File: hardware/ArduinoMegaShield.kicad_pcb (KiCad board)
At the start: 2 copper layers, 42 parts, among them P1 CONN_01X02, P10 CONN_01X02, P11 CONN_01X02, P12 CONN_01X02, P13 CONN_01X02, P14 CONN_01X02, P15 CONN_01X02, P16 CONN_01X02, P17 CONN_01X02, P18 CONN_01X02, P19 CONN_01X02, P2 CONN_01X02, P20 CONN_01X02, P21 CONN_01X02, P22 CONN_01X02, P3 CONN_01X02, P4 CONN_01X02, P5 CONN_01X02, P6 CONN_01X02, P7 CONN_01X02, P8 CONN_01X02, P9 CONN_01X02, U1 A4988, U2 A4988, U3 A4988

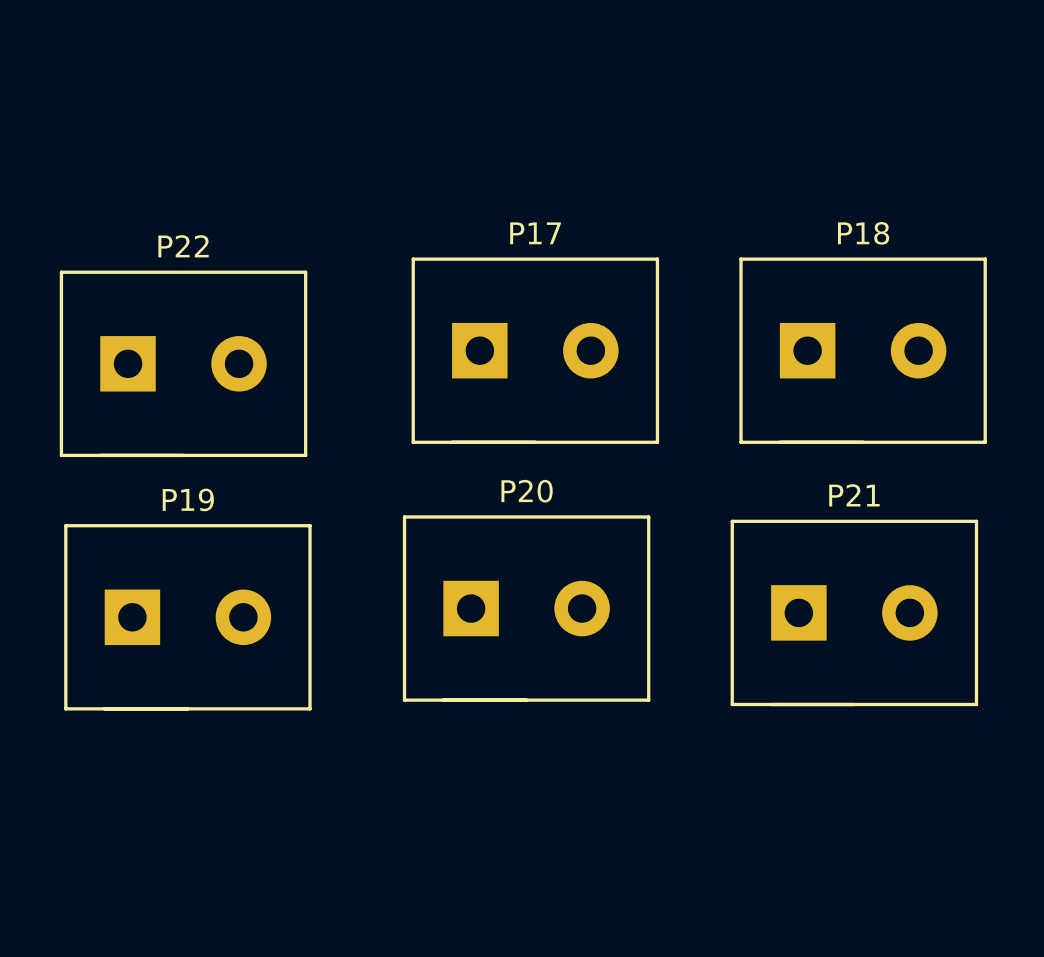
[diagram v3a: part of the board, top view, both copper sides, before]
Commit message: added NOPOPs for optional pullups on limit switches
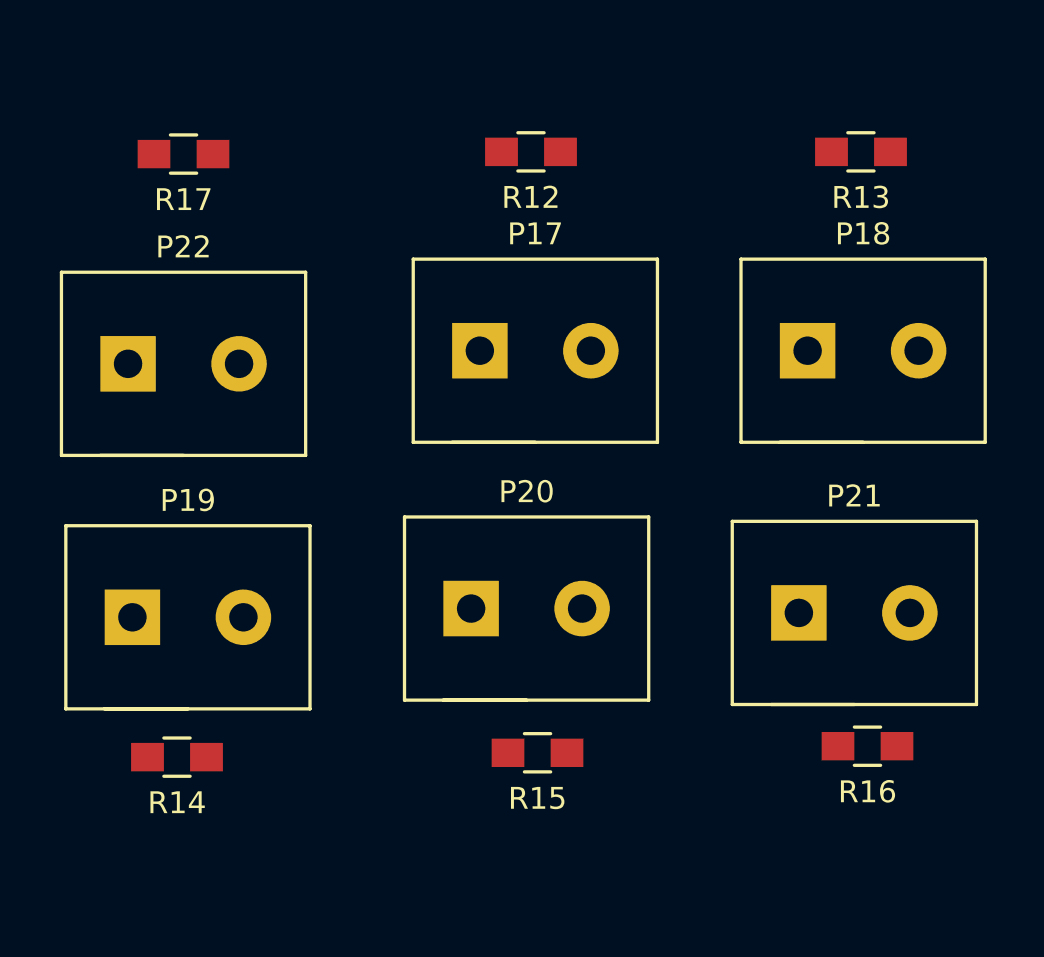
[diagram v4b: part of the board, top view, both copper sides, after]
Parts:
- added R12: NOPOP, Resistors_SMD:R_0805_HandSoldering, F.Cu at (170.0, 137.3)
- added R13: NOPOP, Resistors_SMD:R_0805_HandSoldering, F.Cu at (185.1, 137.3)
- added R14: NOPOP, Resistors_SMD:R_0805_HandSoldering, F.Cu at (153.8, 165.0)
- added R15: NOPOP, Resistors_SMD:R_0805_HandSoldering, F.Cu at (170.3, 164.8)
- added R16: NOPOP, Resistors_SMD:R_0805_HandSoldering, F.Cu at (185.4, 164.5)
- added R17: NOPOP, Resistors_SMD:R_0805_HandSoldering, F.Cu at (154.1, 137.4)
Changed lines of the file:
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@@
 (kicad_pcb (version 4) (host pcbnew 4.0.5)
   (general
-    (links 98)
-    (no_connects 93)
+    (links 110)
+    (no_connects 105)
     (area 0 0 0 0)
     (thickness 1.6)
@@
     (tracks 0)
     (zones 0)
-    (modules 42)
+    (modules 48)
     (nets 46)
   )
@@
       (at (xyz 0 0 0))
       (scale (xyz 1 1 1))
+      (rotate (xyz 0 0 0))
+    )
+  )
+  (module Resistors_SMD:R_0805_HandSoldering (layer F.Cu)
+    (at 170 137.3 180)
+    (descr "Resistor SMD 0805, hand soldering")
+    (tags "resistor 0805")
+    (attr smd)
+    (fp_text reference R12 (at 0 -2.1 180) (layer F.SilkS)
+      (effects (font (size 1 1) (thickness 0.15)))
+    )
+    (fp_text value NOPOP (at 0 2.1 180) (layer F.Fab)
+      (effects (font (size 1 1) (thickness 0.15)))
+    )
+    (fp_line (start -1 0.625) (end -1 -0.625) (layer F.Fab) (width 0.1))
+    (fp_line (start 1 0.625) (end -1 0.625) (layer F.Fab) (width 0.1))
+    (fp_line (start 1 -0.625) (end 1 0.625) (layer F.Fab) (width 0.1))
+    (fp_line (start -1 -0.625) (end 1 -0.625) (layer F.Fab) (width 0.1))
+    (fp_line (start -2.4 -1) (end 2.4 -1) (layer F.CrtYd) (width 0.05))
+    (fp_line (start -2.4 1) (end 2.4 1) (layer F.CrtYd) (width 0.05))
+    (fp_line (start -2.4 -1) (end -2.4 1) (layer F.CrtYd) (width 0.05))
+    (fp_line (start 2.4 -1) (end 2.4 1) (layer F.CrtYd) (width 0.05))
+    (fp_line (start 0.6 0.875) (end -0.6 0.875) (layer F.SilkS) (width 0.15))
+    (fp_line (start -0.6 -0.875) (end 0.6 -0.875) (layer F.SilkS) (width 0.15))
+    (pad 1 smd rect (at -1.35 0 180) (size 1.5 1.3) (layers F.Cu F.Paste F.Mask)
+      (net 7 +5V))
+    (pad 2 smd rect (at 1.35 0 180) (size 1.5 1.3) (layers F.Cu F.Paste F.Mask)
+      (net 40 /A_LIMIT))
+    (model Resistors_SMD.3dshapes/R_0805_HandSoldering.wrl
+      (at (xyz 0 0 0))
+      (scale (xyz 1 1 1))
+      (rotate (xyz 0 0 0))
+    )
+  )
+  (module Resistors_SMD:R_0805_HandSoldering (layer F.Cu)
+    (at 185.1 137.3 180)
+    (descr "Resistor SMD 0805, hand soldering")
+    (tags "resistor 0805")
+    (attr smd)
+    (fp_text reference R13 (at 0 -2.1 180) (layer F.SilkS)
+      (effects (font (size 1 1) (thickness 0.15)))
+    )
+    (fp_text value NOPOP (at 0 2.1 180) (layer F.Fab)
+      (effects (font (size 1 1) (thickness 0.15)))
+    )
+    (fp_line (start -1 0.625) (end -1 -0.625) (layer F.Fab) (width 0.1))
+    (fp_line (start 1 0.625) (end -1 0.625) (layer F.Fab) (width 0.1))
+    (fp_line (start 1 -0.625) (end 1 0.625) (layer F.Fab) (width 0.1))
+    (fp_line (start -1 -0.625) (end 1 -0.625) (layer F.Fab) (width 0.1))
+    (fp_line (start -2.4 -1) (end 2.4 -1) (layer F.CrtYd) (width 0.05))
+    (fp_line (start -2.4 1) (end 2.4 1) (layer F.CrtYd) (width 0.05))
+    (fp_line (start -2.4 -1) (end -2.4 1) (layer F.CrtYd) (width 0.05))
+    (fp_line (start 2.4 -1) (end 2.4 1) (layer F.CrtYd) (width 0.05))
+    (fp_line (start 0.6 0.875) (end -0.6 0.875) (layer F.SilkS) (width 0.15))
+    (fp_line (start -0.6 -0.875) (end 0.6 -0.875) (layer F.SilkS) (width 0.15))
+    (pad 1 smd rect (at -1.35 0 180) (size 1.5 1.3) (layers F.Cu F.Paste F.Mask)
+      (net 7 +5V))
+    (pad 2 smd rect (at 1.35 0 180) (size 1.5 1.3) (layers F.Cu F.Paste F.Mask)
+      (net 41 /X_LIMIT))
+    (model Resistors_SMD.3dshapes/R_0805_HandSoldering.wrl
+      (at (xyz 0 0 0))
+      (scale (xyz 1 1 1))
+      (rotate (xyz 0 0 0))
+    )
+  )
+  (module Resistors_SMD:R_0805_HandSoldering (layer F.Cu)
+    (at 153.8 165 180)
+    (descr "Resistor SMD 0805, hand soldering")
+    (tags "resistor 0805")
+    (attr smd)
+    (fp_text reference R14 (at 0 -2.1 180) (layer F.SilkS)
+      (effects (font (size 1 1) (thickness 0.15)))
+    )
+    (fp_text value NOPOP (at 0 2.1 180) (layer F.Fab)
+      (effects (font (size 1 1) (thickness 0.15)))
+    )
+    (fp_line (start -1 0.625) (end -1 -0.625) (layer F.Fab) (width 0.1))
+    (fp_line (start 1 0.625) (end -1 0.625) (layer F.Fab) (width 0.1))
+    (fp_line (start 1 -0.625) (end 1 0.625) (layer F.Fab) (width 0.1))
+    (fp_line (start -1 -0.625) (end 1 -0.625) (layer F.Fab) (width 0.1))
+    (fp_line (start -2.4 -1) (end 2.4 -1) (layer F.CrtYd) (width 0.05))
+    (fp_line (start -2.4 1) (end 2.4 1) (layer F.CrtYd) (width 0.05))
+    (fp_line (start -2.4 -1) (end -2.4 1) (layer F.CrtYd) (width 0.05))
+    (fp_line (start 2.4 -1) (end 2.4 1) (layer F.CrtYd) (width 0.05))
+    (fp_line (start 0.6 0.875) (end -0.6 0.875) (layer F.SilkS) (width 0.15))
+    (fp_line (start -0.6 -0.875) (end 0.6 -0.875) (layer F.SilkS) (width 0.15))
+    (pad 1 smd rect (at -1.35 0 180) (size 1.5 1.3) (layers F.Cu F.Paste F.Mask)
+      (net 7 +5V))
+    (pad 2 smd rect (at 1.35 0 180) (size 1.5 1.3) (layers F.Cu F.Paste F.Mask)
+      (net 42 /B_LIMIT))
+    (model Resistors_SMD.3dshapes/R_0805_HandSoldering.wrl
+      (at (xyz 0 0 0))
+      (scale (xyz 1 1 1))
+      (rotate (xyz 0 0 0))
+    )
+  )
+  (module Resistors_SMD:R_0805_HandSoldering (layer F.Cu)
+    (at 170.3 164.8 180)
+    (descr "Resistor SMD 0805, hand soldering")
+    (tags "resistor 0805")
+    (attr smd)
+    (fp_text reference R15 (at 0 -2.1 180) (layer F.SilkS)
+      (effects (font (size 1 1) (thickness 0.15)))
+    )
+    (fp_text value NOPOP (at 0 2.1 180) (layer F.Fab)
+      (effects (font (size 1 1) (thickness 0.15)))
+    )
+    (fp_line (start -1 0.625) (end -1 -0.625) (layer F.Fab) (width 0.1))
+    (fp_line (start 1 0.625) (end -1 0.625) (layer F.Fab) (width 0.1))
+    (fp_line (start 1 -0.625) (end 1 0.625) (layer F.Fab) (width 0.1))
+    (fp_line (start -1 -0.625) (end 1 -0.625) (layer F.Fab) (width 0.1))
+    (fp_line (start -2.4 -1) (end 2.4 -1) (layer F.CrtYd) (width 0.05))
+    (fp_line (start -2.4 1) (end 2.4 1) (layer F.CrtYd) (width 0.05))
+    (fp_line (start -2.4 -1) (end -2.4 1) (layer F.CrtYd) (width 0.05))
+    (fp_line (start 2.4 -1) (end 2.4 1) (layer F.CrtYd) (width 0.05))
+    (fp_line (start 0.6 0.875) (end -0.6 0.875) (layer F.SilkS) (width 0.15))
+    (fp_line (start -0.6 -0.875) (end 0.6 -0.875) (layer F.SilkS) (width 0.15))
+    (pad 1 smd rect (at -1.35 0 180) (size 1.5 1.3) (layers F.Cu F.Paste F.Mask)
+      (net 7 +5V))
+    (pad 2 smd rect (at 1.35 0 180) (size 1.5 1.3) (layers F.Cu F.Paste F.Mask)
+      (net 43 /Y_LIMIT))
+    (model Resistors_SMD.3dshapes/R_0805_HandSoldering.wrl
+      (at (xyz 0 0 0))
+      (scale (xyz 1 1 1))
+      (rotate (xyz 0 0 0))
+    )
+  )
+  (module Resistors_SMD:R_0805_HandSoldering (layer F.Cu)
+    (at 185.4 164.5 180)
+    (descr "Resistor SMD 0805, hand soldering")
+    (tags "resistor 0805")
+    (attr smd)
+    (fp_text reference R16 (at 0 -2.1 180) (layer F.SilkS)
+      (effects (font (size 1 1) (thickness 0.15)))
+    )
+    (fp_text value NOPOP (at 0 2.1 180) (layer F.Fab)
+      (effects (font (size 1 1) (thickness 0.15)))
+    )
+    (fp_line (start -1 0.625) (end -1 -0.625) (layer F.Fab) (width 0.1))
+    (fp_line (start 1 0.625) (end -1 0.625) (layer F.Fab) (width 0.1))
+    (fp_line (start 1 -0.625) (end 1 0.625) (layer F.Fab) (width 0.1))
+    (fp_line (start -1 -0.625) (end 1 -0.625) (layer F.Fab) (width 0.1))
+    (fp_line (start -2.4 -1) (end 2.4 -1) (layer F.CrtYd) (width 0.05))
+    (fp_line (start -2.4 1) (end 2.4 1) (layer F.CrtYd) (width 0.05))
+    (fp_line (start -2.4 -1) (end -2.4 1) (layer F.CrtYd) (width 0.05))
+    (fp_line (start 2.4 -1) (end 2.4 1) (layer F.CrtYd) (width 0.05))
+    (fp_line (start 0.6 0.875) (end -0.6 0.875) (layer F.SilkS) (width 0.15))
+    (fp_line (start -0.6 -0.875) (end 0.6 -0.875) (layer F.SilkS) (width 0.15))
+    (pad 1 smd rect (at -1.35 0 180) (size 1.5 1.3) (layers F.Cu F.Paste F.Mask)
+      (net 7 +5V))
+    (pad 2 smd rect (at 1.35 0 180) (size 1.5 1.3) (layers F.Cu F.Paste F.Mask)
+      (net 44 /C_LIMIT))
+    (model Resistors_SMD.3dshapes/R_0805_HandSoldering.wrl
+      (at (xyz 0 0 0))
+      (scale (xyz 1 1 1))
+      (rotate (xyz 0 0 0))
+    )
+  )
+  (module Resistors_SMD:R_0805_HandSoldering (layer F.Cu)
+    (at 154.1 137.4 180)
+    (descr "Resistor SMD 0805, hand soldering")
+    (tags "resistor 0805")
+    (attr smd)
+    (fp_text reference R17 (at 0 -2.1 180) (layer F.SilkS)
+      (effects (font (size 1 1) (thickness 0.15)))
+    )
+    (fp_text value NOPOP (at 0 2.1 180) (layer F.Fab)
+      (effects (font (size 1 1) (thickness 0.15)))
+    )
+    (fp_line (start -1 0.625) (end -1 -0.625) (layer F.Fab) (width 0.1))
+    (fp_line (start 1 0.625) (end -1 0.625) (layer F.Fab) (width 0.1))
+    (fp_line (start 1 -0.625) (end 1 0.625) (layer F.Fab) (width 0.1))
+    (fp_line (start -1 -0.625) (end 1 -0.625) (layer F.Fab) (width 0.1))
+    (fp_line (start -2.4 -1) (end 2.4 -1) (layer F.CrtYd) (width 0.05))
+    (fp_line (start -2.4 1) (end 2.4 1) (layer F.CrtYd) (width 0.05))
+    (fp_line (start -2.4 -1) (end -2.4 1) (layer F.CrtYd) (width 0.05))
+    (fp_line (start 2.4 -1) (end 2.4 1) (layer F.CrtYd) (width 0.05))
+    (fp_line (start 0.6 0.875) (end -0.6 0.875) (layer F.SilkS) (width 0.15))
+    (fp_line (start -0.6 -0.875) (end 0.6 -0.875) (layer F.SilkS) (width 0.15))
+    (pad 1 smd rect (at -1.35 0 180) (size 1.5 1.3) (layers F.Cu F.Paste F.Mask)
+      (net 7 +5V))
+    (pad 2 smd rect (at 1.35 0 180) (size 1.5 1.3) (layers F.Cu F.Paste F.Mask)
+      (net 45 /Z_LIMIT))
+    (model Resistors_SMD.3dshapes/R_0805_HandSoldering.wrl
+      (at (xyz 0 0 0))
+      (scale (xyz 1 1 1))
